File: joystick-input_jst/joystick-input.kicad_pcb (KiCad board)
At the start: 2 copper layers, 71.4 x 39.2 mm, 38 parts, among them J1 Conn_01x05, J10 Conn_01x02, J11 Conn_01x02, J12 Conn_01x02, J13 Conn_01x02, J14 Conn_01x02, J15 Conn_01x02, J16 Conn_01x02, J17 Conn_01x02, J18 Conn_01x02, J19 Conn_01x02, J2 Conn_01x02, J20 Conn_01x02, J21 Conn_01x02, J22 Conn_01x02, J3 Conn_01x05, J4 Conn_01x02, J5 Conn_01x02, J6 Conn_01x02, J7 Conn_01x02, J8 Conn_01x02, J9 Conn_01x02

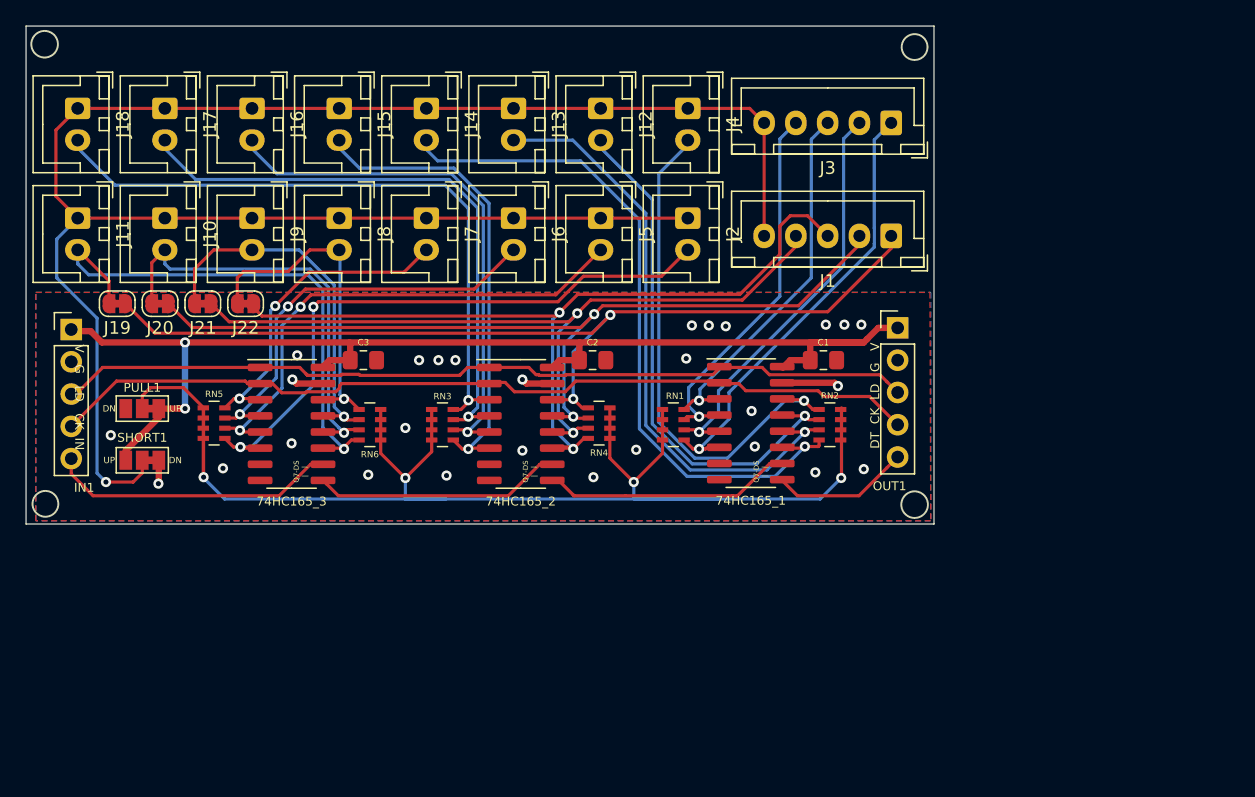
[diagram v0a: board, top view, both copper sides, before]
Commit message: joystick_input_jst 업데이트
Signed-off-by: Ju, Gyeong-min <jcmh74@gmail.com>
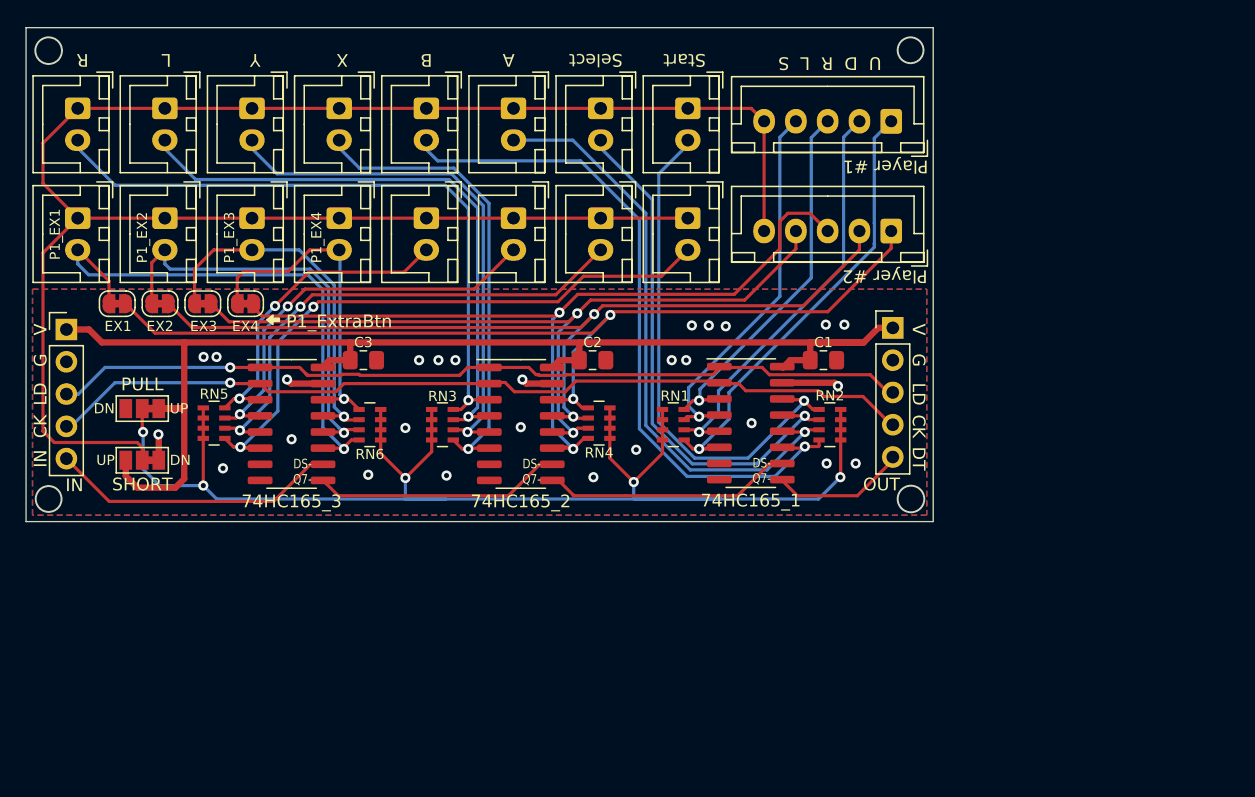
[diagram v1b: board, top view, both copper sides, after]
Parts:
- removed J1: Conn_01x05, Connector_JST:JST_XH_B5B-XH-A_1x05_P2.50mm_Vertical
- added J21: Conn_01x05, Connector_JST:JST_XH_B5B-XH-A_1x05_P2.50mm_Vertical, F.Cu at (161.8, 74.2)
- moved IN1 0.38 mm to (96.9, 81.9)
- moved OUT1 0.38 mm to (161.9, 81.8)
- moved J11 0.13 mm to (161.8, 65.5)
- renumbered J3 to J11, J4 to J12, J12 to J13, J13 to J14, J14 to J15, J15 to J16, J16 to J17, J17 to J18, J18 to J19, J2 to J22, J5 to J23, J6 to J24, J7 to J25, J8 to J26, J9 to J27, J10 to J28, J11 to J29, PULL1 to JP1, SHORT1 to JP2, J19 to JP3, J20 to JP4, J21 to JP5, J22 to JP6
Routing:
- net VCC: track 94.5 -> 102.8 mm, vias 2 -> 0
- net /PULL: track 113.4 -> 111.4 mm, vias 4 -> 5
- net /CLK: track 69.4 -> 70.1 mm, vias 0 -> 1
- net /C_P2_DOWN: track 70.6 -> 71.2 mm
- net GND: track 11.4 -> 12.0 mm, vias 28 -> 27
- net /C_SHORT: track 148.6 -> 149.2 mm, vias 1 -> 0
- net /LOAD: vias 0 -> 1
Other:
- board size 71.4 x 39.2 mm -> 71.4 x 38.9 mm
- board text added: "A"
- board text added: "B"
- board text added: "CK"
- board text added: "DS- Q7-"
- board text added: "DT"
- board text added: "EX1"
- board text added: "EX2"
- board text added: "EX3"
- board text added: "EX4"
- board text added: "G"
- board text added: "IN"
- board text added: "L"
- board text added: "LD"
- board text added: "OUT"
- board text added: "P1_EX1"
- board text added: "P1_EX2"
- board text added: "P1_EX3"
- board text added: "P1_EX4"
- board text added: "P1_ExtraBtn"
- board text added: "PULL"
- board text added: "Player #1"
- board text added: "Player #2"
- board text added: "R"
- board text added: "Rev.3"
- board text added: "SHORT"
- board text added: "Select"
- board text added: "Start"
- board text added: "U D R L S"
- board text added: "V"
- board text added: "X"
- board text added: "Y"
- board text removed: "DT CK LD G V"
- board text removed: "Q7-DS | |"
- board text removed: "Rev.2"
- board text removed: "V G LD CK IN"

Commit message: 불필요한 파일들 삭제
Signed-off-by: Ju, Gyeong-min <jcmh74@gmail.com>
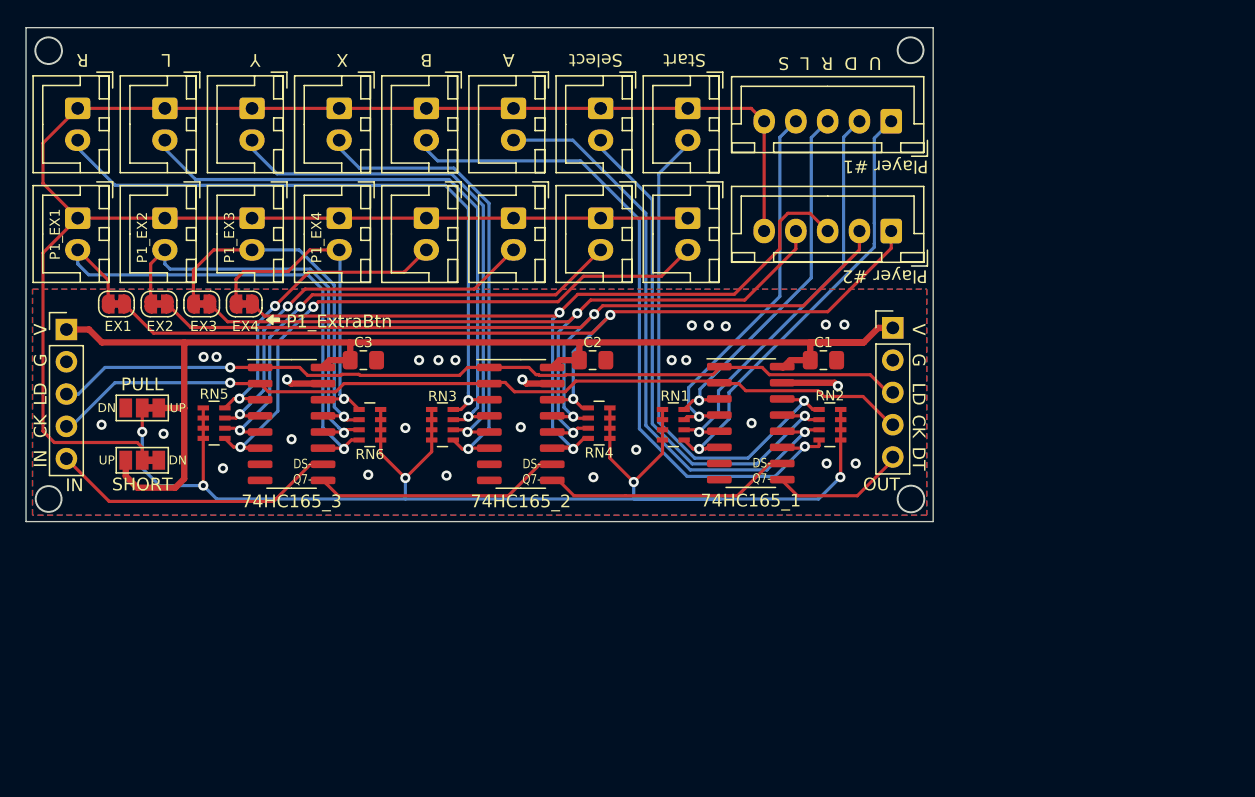
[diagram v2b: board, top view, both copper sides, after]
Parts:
- moved JP6 0.10 mm to (110.9, 79.9)
- moved JP5 0.09 mm to (107.5, 79.9)
- moved JP4 0.08 mm to (104.2, 79.9)
- moved JP3 0.07 mm to (100.8, 79.9)
- moved JP1 0.05 mm to (102.9, 88.1)
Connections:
- 74HC165_1 pad 7: (no net) -> unconnected-(74HC165_1-Pad7)
- 74HC165_2 pad 7: (no net) -> unconnected-(74HC165_2-Pad7)
- 74HC165_3 pad 7: (no net) -> unconnected-(74HC165_3-Pad7)
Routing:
- net /PULL: track 111.4 -> 108.2 mm
- net GND: track 12.0 -> 9.93 mm, vias 27 -> 28
- net VCC: track 102.8 -> 100.9 mm
- net /CLK: track 70.1 -> 69.2 mm
- net /C_P1_X: track 38.2 -> 37.4 mm
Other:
- net class Default removed
- net class Power removed

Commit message: 도면 시트 설명 추가
Signed-off-by: Ju, Gyeong-min <jcmh74@gmail.com>
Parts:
- moved J25 30.4 mm to (148.5, 92.8)
- moved J15 30.4 mm to (148.5, 84.1)
- moved 74HC165_2 30.4 mm to (155.9, 109.0)
- moved 74HC165_3 30.4 mm to (137.9, 109.0)
- moved C1 30.4 mm to (179.7, 103.9)
- moved C2 30.4 mm to (161.6, 103.9)
- moved C3 30.4 mm to (143.5, 103.9)
- moved J11 30.4 mm to (185.1, 85.1)
- moved J22 30.4 mm to (169.1, 92.8)
- moved J23 30.4 mm to (162.2, 92.8)
- moved J26 30.4 mm to (141.6, 92.8)
- moved J27 30.4 mm to (134.8, 92.8)
- moved J28 30.4 mm to (127.9, 92.8)
- moved JP3 30.4 mm to (124.1, 99.5)
- moved JP4 30.4 mm to (127.5, 99.5)
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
